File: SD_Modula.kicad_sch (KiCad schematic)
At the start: 6 parts, among them J2 Micro_SD_Card_Det1, U4 74LVC125

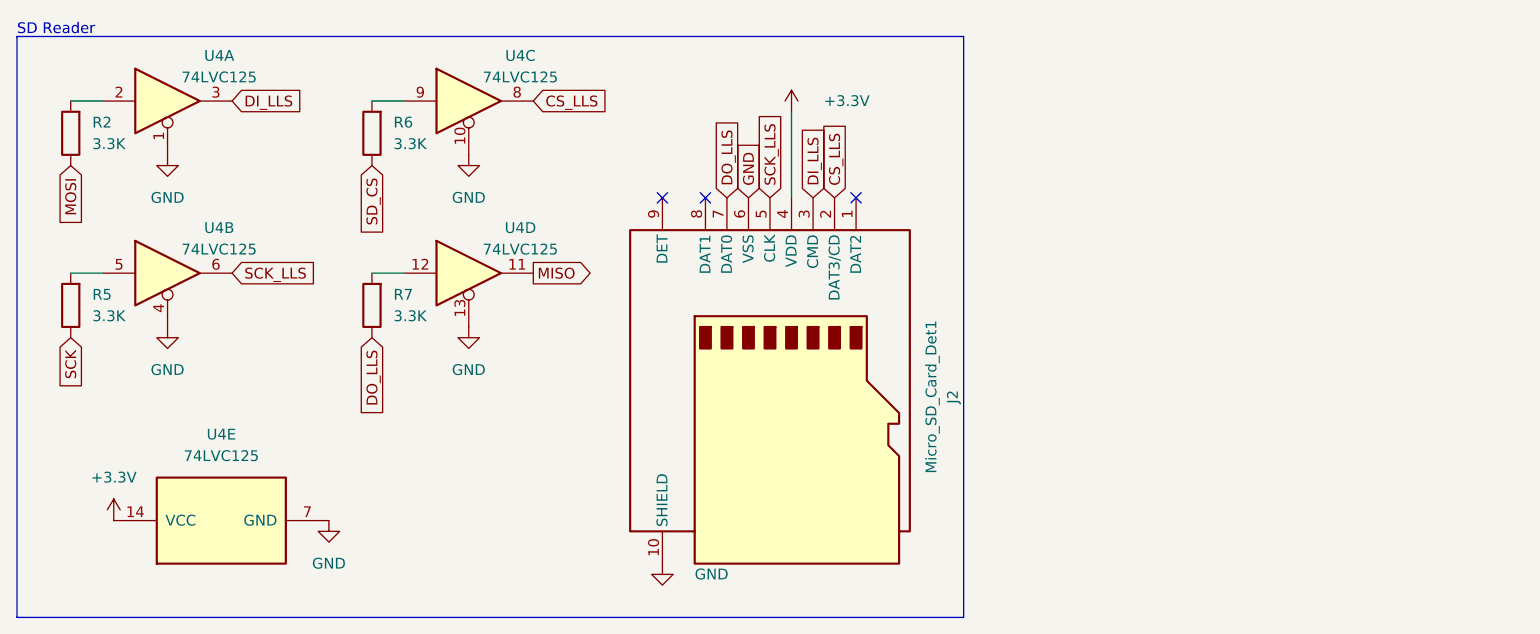
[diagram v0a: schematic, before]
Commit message: added psu and formated board outline
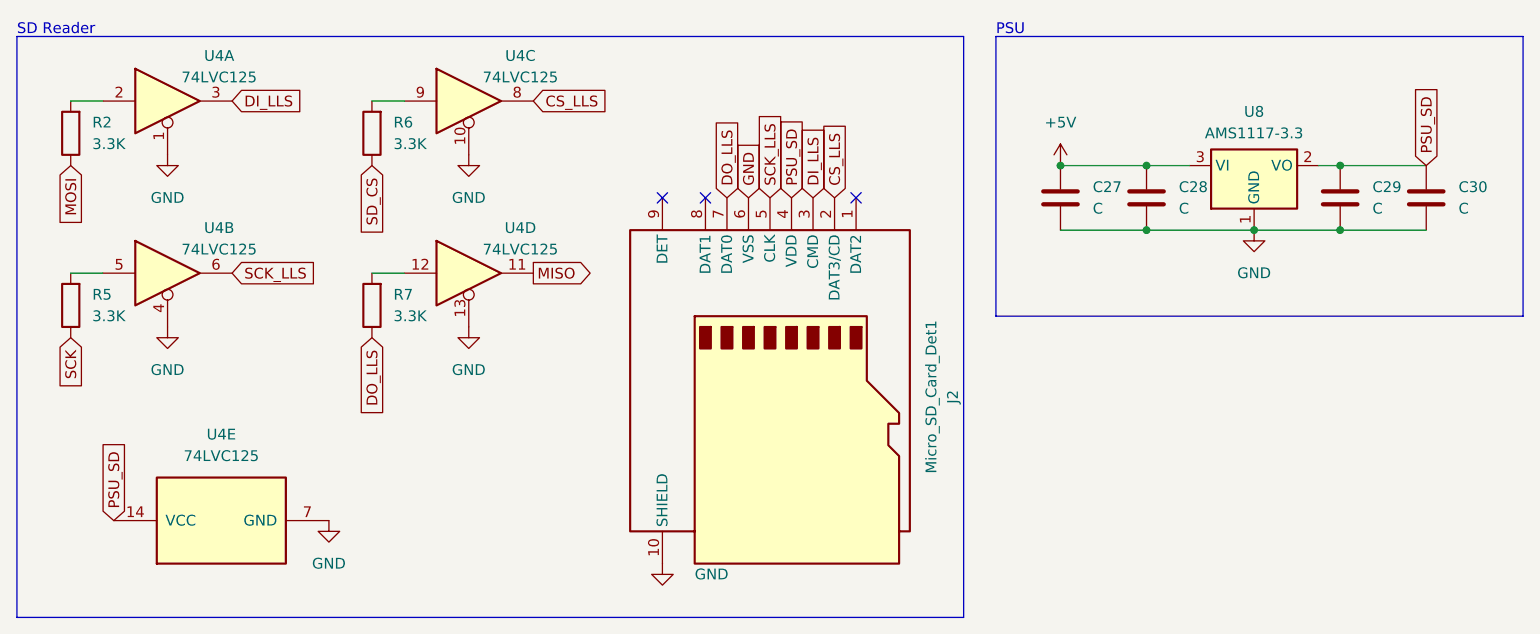
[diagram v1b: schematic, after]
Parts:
- added C27, C28, C29, C30: C, symbol Device:C
- added U8: AMS1117-3.3, Package_TO_SOT_SMD:SOT-223-3_TabPin2, symbol Regulator_Linear:AMS1117-3.3
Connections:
- net GND: now also C27.2, C28.2, C29.2, C30.2, U8.1 (GND)
- net +3.3V renamed PSU_SD
- net PSU_SD: now also C29.1, C30.1, U8.2 (VO)
- new net +5V: C27.1, C28.1, U8.3 (VI)
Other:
- note added: "PSU"

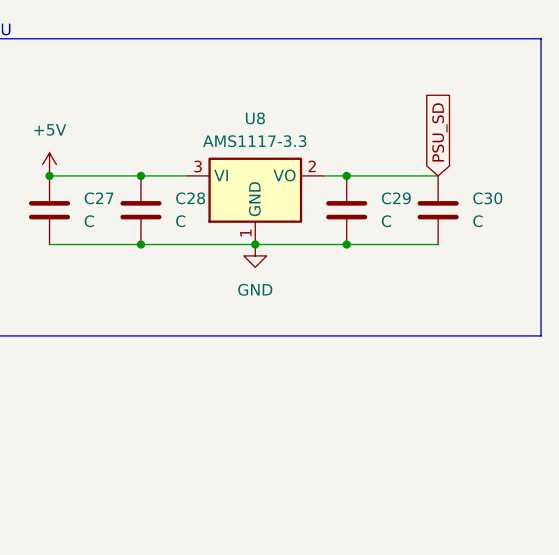
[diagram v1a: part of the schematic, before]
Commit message: added footprint for a7670e
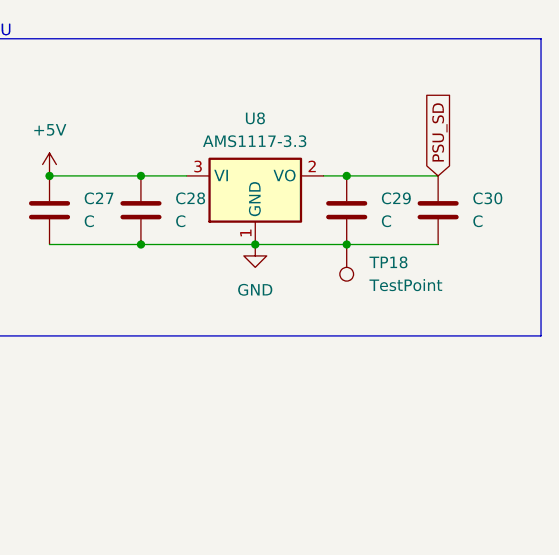
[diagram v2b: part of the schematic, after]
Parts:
- added TP18: TestPoint, symbol Connector:TestPoint
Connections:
- net GND: now also TP18.1
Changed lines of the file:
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@@
+	)
+	(symbol
+		(lib_id "Connector:TestPoint")
+		(at 173.99 40.64 180)
+		(unit 1)
+		(exclude_from_sim no)
+		(in_bom yes)
+		(on_board yes)
+		(dnp no)
+		(fields_autoplaced yes)
+		(property "Reference" "TP18"
+			(at 176.53 42.6719 0)
+			(effects
+				(font
+					(size 1.27 1.27)
+				)
+				(justify right)
+			)
+		)
+		(property "Value" "TestPoint"
+			(at 176.53 45.2119 0)
+			(effects
+				(font
+					(size 1.27 1.27)
+				)
+				(justify right)
+			)
+		)
+		(property "Footprint" ""
+			(at 168.91 40.64 0)
+			(effects
+				(font
+					(size 1.27 1.27)
+				)
+				(hide yes)
+			)
+		)
+		(property "Datasheet" "~"
+			(at 168.91 40.64 0)
+			(effects
+				(font
+					(size 1.27 1.27)
+				)
+				(hide yes)
+			)
+		)
+		(property "Description" "test point"
+			(at 173.99 40.64 0)
+			(effects
+				(font
+					(size 1.27 1.27)
+				)
+				(hide yes)
+			)
+		)
+		(pin "1"
+		)
+		(instances
+			(project "Hardware"
+				(path "/f04ee758-a926-48b7-b458-286a696c3ef4/9702ddf2-9814-4139-b4ef-da102dfdd360"
+					(reference "TP18")
+					(unit 1)
+				)
+			)
+		)
 	)
 	(symbol

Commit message: done most of the schematics
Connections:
- net PSU_SD renamed PSU
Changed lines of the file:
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@@
+		)
+	)
+	(wire
+		(pts
+			(xy 109.22 25.4) (xy 109.22 36.83)
+		)
+		(stroke
+			(width 0)
+			(type default)
 		)
 	)
@@
 		)
 	)
+	(label "PSU"
+		(at 184.15 33.02 180)
+		(fields_autoplaced yes)
+		(effects
+			(font
+				(size 1.27 1.27)
+			)
+			(justify right bottom)
+		)
+	)
+	(label "PSU"
+		(at 29.21 74.93 180)
+		(fields_autoplaced yes)
+		(effects
+			(font
+				(size 1.27 1.27)
+			)
+			(justify right bottom)
+		)
+	)
+	(label "PSU"
+		(at 109.22 25.4 90)
+		(fields_autoplaced yes)
+		(effects
+			(font
+				(size 1.27 1.27)
+			)
+			(justify left bottom)
+		)
+	)
 	(global_label "SCK_LLS"
 		(shape input)
@@
 		(property "Intersheetrefs" "${INTERSHEET_REFS}"
 			(at 106.68 25.862 90)
-			(effects
-				(font
-					(size 1.27 1.27)
-				)
-				(justify left)
-				(hide yes)
-			)
-		)
-	)
-	(global_label "PSU_SD"
-		(shape input)
-		(at 29.21 74.93 90)
-		(fields_autoplaced yes)
-		(effects
-			(font
-				(size 1.27 1.27)
-			)
-			(justify left)
-		)
-		(property "Intersheetrefs" "${INTERSHEET_REFS}"
-			(at 29.21 64.6877 90)
 			(effects
 				(font
@@
 		)
 	)
-	(global_label "PSU_SD"
-		(shape input)
-		(at 184.15 33.02 90)
-		(fields_autoplaced yes)
-		(effects
-			(font
-				(size 1.27 1.27)
-			)
-			(justify left)
-		)
-		(property "Intersheetrefs" "${INTERSHEET_REFS}"
-			(at 184.15 22.7777 90)
-			(effects
-				(font
-					(size 1.27 1.27)
-				)
-				(justify left)
-				(hide yes)
-			)
-		)
-	)
 	(global_label "SD_CS"
 		(shape input)
@@
 			(effects
 				(font
-					(size 1.27 1.27)
-				)
-				(justify left)
-				(hide yes)
-			)
-		)
-	)
-	(global_label "PSU_SD"
-		(shape input)
-		(at 109.22 36.83 90)
-		(fields_autoplaced yes)
-		(effects
-			(font
-				(size 1.27 1.27)
-			)
-			(justify left)
-		)
-		(property "Intersheetrefs" "${INTERSHEET_REFS}"
-			(at 109.22 26.5877 90)
-			(effects
-				(font

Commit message: done refacoring
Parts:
- C27, C29: value C -> 10uF
- C28, C30: value C -> 100pF
- TP18: footprint (none) -> TestPoint:TestPoint_Pad_D2.5mm

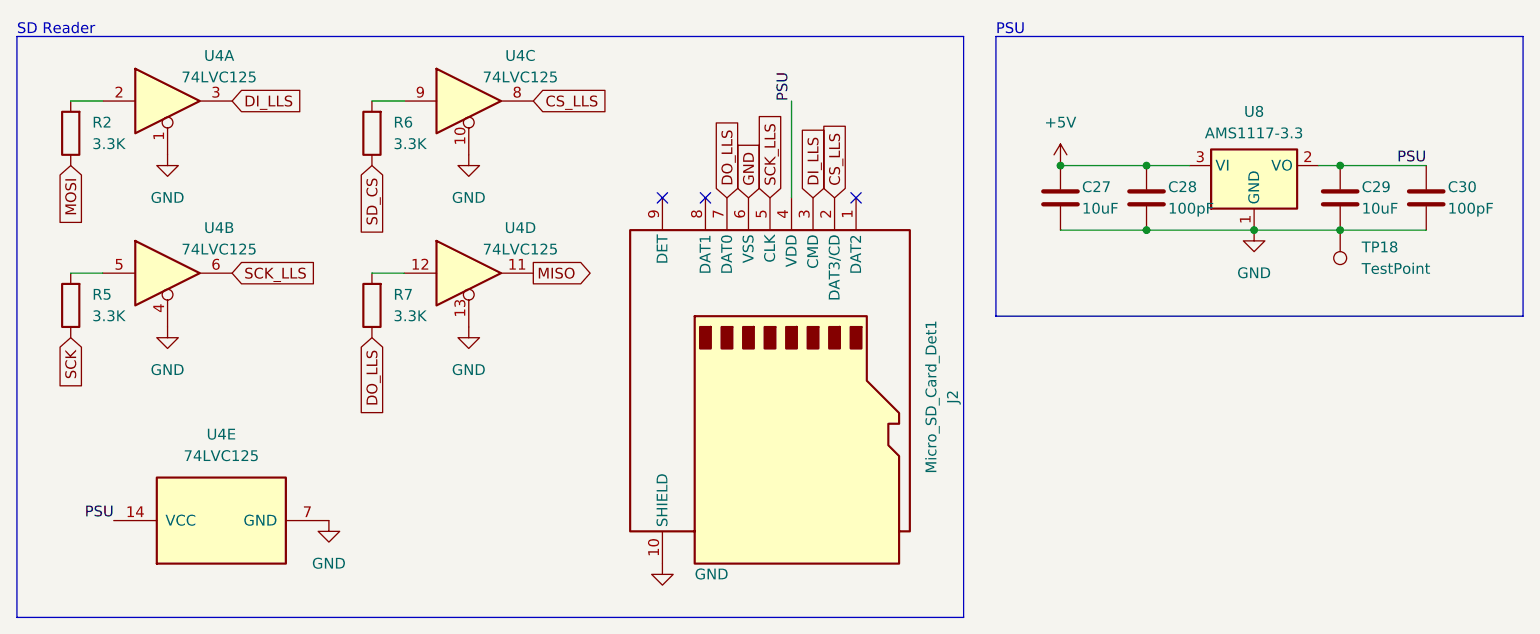
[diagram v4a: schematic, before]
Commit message: assigned most footprints
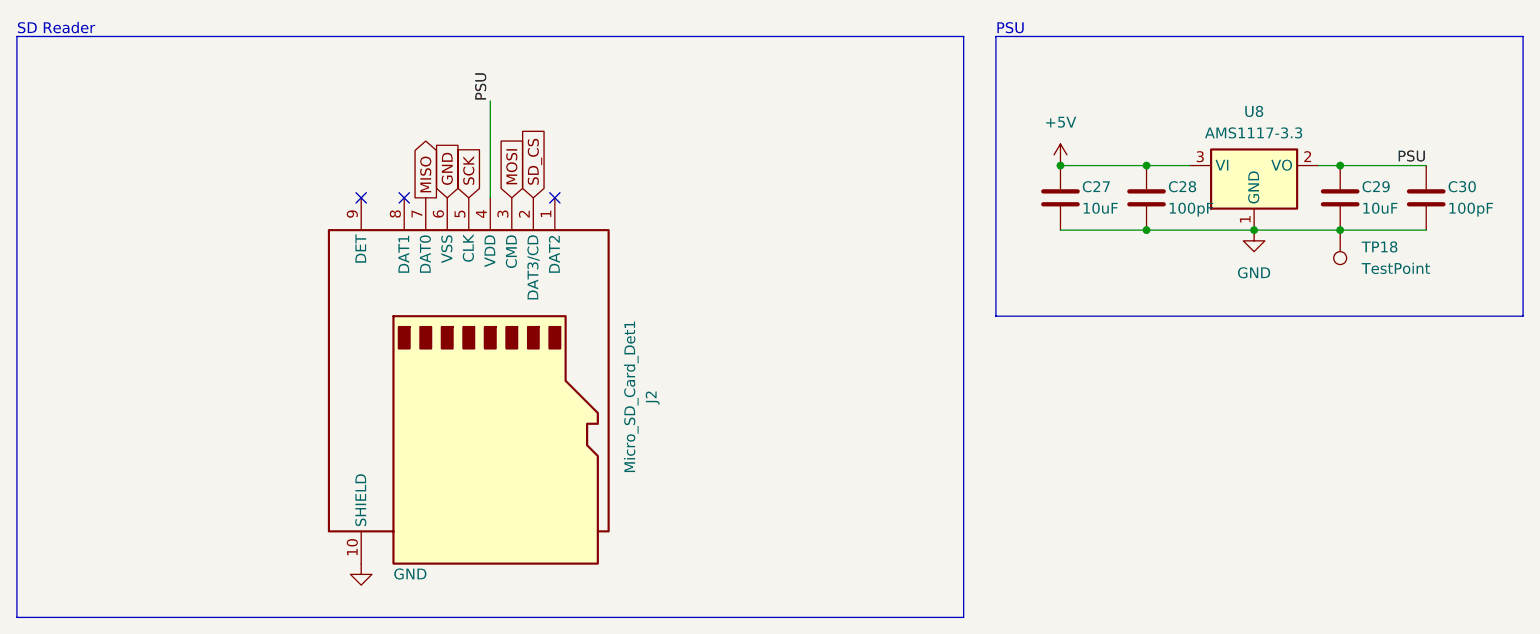
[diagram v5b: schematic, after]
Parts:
- removed R2, R5, R6, R7: 3.3K, symbol Device:R
- removed U4: 74LVC125, symbol 74xx:74LVC125
- J2: footprint (none) -> 3M_SD-RSMT-2-MQ-WF:3M_SD-RSMT-2-MQ-WF
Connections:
- net CS_LLS is gone; now on net SD_CS: J2.2 (DAT3/CD)
- net DI_LLS is gone; now on net MOSI: J2.3 (CMD)
- net DO_LLS is gone; now on net MISO: J2.7 (DAT0)
- net SCK_LLS is gone; now on net SCK: J2.5 (CLK)
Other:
- moved on the sheet: J2

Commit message: cleaned up scematics and updated power management
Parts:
- C27, C29: footprint (none) -> Capacitor_SMD:C_1206_3216Metric
- C28, C30: footprint (none) -> Capacitor_SMD:C_0805_2012Metric

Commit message: finelized scematics
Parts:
- removed J2: Micro_SD_Card_Det1, 3M_SD-RSMT-2-MQ-WF:3M_SD-RSMT-2-MQ-WF, symbol Connector:Micro_SD_Card_Det1
- added J6: Micro_SD_Card, Connector_Card:microSD_HC_Hirose_DM3BT-DSF-PEJS, symbol Connector:Micro_SD_Card
- TP18: footprint TestPoint:TestPoint_Pad_D2.5mm -> TestPoint:TestPoint_Pad_D2.0mm
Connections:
- net GND: now also J6.6 (VSS), J6.9 (SHIELD)
- net MISO: now also J6.7 (DAT0)
- net MOSI: now also J6.3 (CMD)
- net PSU: now also J6.4 (VDD)
- net SCK: now also J6.5 (CLK)
- net SD_CS: now also J6.2 (DAT3/CD)
- no-connect marks 3 -> 2
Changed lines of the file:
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@@
 		(at 63.5 36.83)
-	)
-	(no_connect
-		(at 58.42 36.83)
 	)
 	(wire
@@
 	)
 	(symbol
+		(lib_id "Connector:Micro_SD_Card")
+		(at 73.66 59.69 270)
+		(unit 1)
+		(exclude_from_sim no)
+		(in_bom yes)
+		(on_board yes)
+		(dnp no)
+		(fields_autoplaced yes)
+		(property "Reference" "J6"
+			(at 88.9 59.0549 90)
+			(effects
+				(font
+					(size 1.27 1.27)
+				)
+				(justify left)
+			)
+		)
+		(property "Value" "Micro_SD_Card"
+			(at 88.9 61.5949 90)
+			(effects
+				(font
+					(size 1.27 1.27)
+				)
+				(justify left)
+			)
+		)
+		(property "Footprint" "Connector_Card:microSD_HC_Hirose_DM3BT-DSF-PEJS"
+			(at 81.28 88.9 0)
+			(effects
+				(font
+					(size 1.27 1.27)
+				)
+				(hide yes)
+			)
+		)
+		(property "Datasheet" "http://katalog.we-online.de/em/datasheet/693072010801.pdf"
+			(at 73.66 59.69 0)
+			(effects
+				(font
+					(size 1.27 1.27)
+				)
+				(hide yes)
+			)
+		)
+		(property "Description" "Micro SD Card Socket"
+			(at 73.66 59.69 0)
+			(effects
+				(font
+					(size 1.27 1.27)
+				)
+				(hide yes)
+			)
+		)
+		(pin "2"
+		)
+		(pin "8"
+		)
+		(pin "7"
+		)
+		(pin "5"
+		)
+		(pin "3"
+		)
+		(pin "1"
+		)
+		(pin "4"
+		)
+		(pin "6"
+		)
+		(pin "9"
+		)
+		(instances
+			(project "Hardware"
+				(path "/f04ee758-a926-48b7-b458-286a696c3ef4/9702ddf2-9814-4139-b4ef-da102dfdd360"
+					(reference "J6")
+					(unit 1)
+				)
+			)
+		)
+	)
+	(symbol
 		(lib_id "Device:C")
 		(at 151.13 36.83 0)
@@
 	)
 	(symbol
-		(lib_id "Connector:Micro_SD_Card_Det1")
-		(at 71.12 59.69 270)
-		(unit 1)
-		(exclude_from_sim no)
-		(in_bom yes)
-		(on_board yes)
-		(dnp no)
-		(fields_autoplaced yes)
-		(property "Reference" "J2"
-			(at 92.71 60.325 0)
-			(effects
-				(font
-					(size 1.27 1.27)
-				)
-			)
-		)
-		(property "Value" "Micro_SD_Card_Det1"
-			(at 90.17 60.325 0)
-			(effects
-				(font
-					(size 1.27 1.27)
-				)
-			)
-		)
-		(property "Footprint" "3M_SD-RSMT-2-MQ-WF:3M_SD-RSMT-2-MQ-WF"
-			(at 88.9 111.76 0)
-			(effects
-				(font
-					(size 1.27 1.27)
-				)
-				(hide yes)
-			)
-		)
-		(property "Datasheet" "https://datasheet.lcsc.com/lcsc/2110151630_XKB-Connectivity-XKTF-015-N_C381082.pdf"
-			(at 73.66 59.69 0)
-			(effects
-				(font
-					(size 1.27 1.27)
-				)
-				(hide yes)
-			)
-		)
-		(property "Description" "Micro SD Card Socket with one card detection pin"
-			(at 71.12 59.69 0)
-			(effects
-				(font
-					(size 1.27 1.27)
-				)
-				(hide yes)
-			)
-		)
-		(property "Availability" ""
-			(at 71.12 59.69 0)
-			(effects
-				(font
-					(size 1.27 1.27)
-				)
-				(hide yes)
-			)
-		)
-		(property "Check_prices" ""
-			(at 71.12 59.69 0)
-			(effects
-				(font
-					(size 1.27 1.27)
-				)
-				(hide yes)
-			)
-		)
-		(property "Description_1" ""
-			(at 71.12 59.69 0)
-			(effects
-				(font
-					(size 1.27 1.27)
-				)
-				(hide yes)
-			)
-		)
-		(property "MANUFACTURER" ""
-			(at 71.12 59.69 0)
-			(effects
-				(font
-					(size 1.27 1.27)
-				)
-				(hide yes)
-			)
-		)
-		(property "MAXIMUM_PACKAGE_HEIGHT" ""
-			(at 71.12 59.69 0)
-			(effects
-				(font
-					(size 1.27 1.27)
-				)
-				(hide yes)
-			)
-		)
-		(property "MF" ""
-			(at 71.12 59.69 0)
-			(effects
-				(font
-					(size 1.27 1.27)
-				)
-				(hide yes)
-			)
-		)
-		(property "MP" ""
-			(at 71.12 59.69 0)
-			(effects
-				(font
-					(size 1.27 1.27)
-				)
-				(hide yes)
-			)
-		)
-		(property "PARTREV" ""
-			(at 71.12 59.69 0)
-			(effects
-				(font
-					(size 1.27 1.27)
-				)
-				(hide yes)
-			)
-		)
-		(property "Package" ""
-			(at 71.12 59.69 0)
-			(effects
-				(font
-					(size 1.27 1.27)
-				)
-				(hide yes)
-			)
-		)
-		(property "Price" ""
-			(at 71.12 59.69 0)
-			(effects
-				(font
-					(size 1.27 1.27)
-				)
-				(hide yes)
-			)
-		)
-		(property "SNAPEDA_PN" ""
-			(at 71.12 59.69 0)
-			(effects
-				(font
-					(size 1.27 1.27)
-				)
-				(hide yes)
-			)
-		)
-		(property "STANDARD" ""
-			(at 71.12 59.69 0)
-			(effects
-				(font
-					(size 1.27 1.27)
-				)
-				(hide yes)
-			)
-		)
-		(property "SnapEDA_Link" ""
-			(at 71.12 59.69 0)
-			(effects
-				(font
-					(size 1.27 1.27)
-				)
-				(hide yes)
-			)
-		)
-		(pin "1"
-		)
-		(pin "9"
-		)
-		(pin "6"
-		)
-		(pin "7"
-		)
-		(pin "3"
-		)
-		(pin "8"
-		)
-		(pin "5"
-		)
-		(pin "2"
-		)
-		(pin "4"
-		)
-		(pin "10"
-		)
-		(instances
-			(project "Hardware"
-				(path "/f04ee758-a926-48b7-b458-286a696c3ef4/9702ddf2-9814-4139-b4ef-da102dfdd360"
-					(reference "J2")
-					(unit 1)
-				)
-			)
-		)
-	)
-	(symbol
 		(lib_id "Connector:TestPoint")
 		(at 173.99 40.64 180)
@@
 			)
 		)
-		(property "Footprint" "TestPoint:TestPoint_Pad_D2.5mm"
+		(property "Footprint" "TestPoint:TestPoint_Pad_D2.0mm"
 			(at 168.91 40.64 0)
 			(effects

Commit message: mostly layouted
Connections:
- net GND: no longer TP18.1
- net PSU: now also TP18.1
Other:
- moved on the sheet: TP18
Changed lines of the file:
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@@
+		)
+	)
+	(wire
+		(pts
+			(xy 173.99 30.48) (xy 173.99 33.02)
+		)
+		(stroke
+			(width 0)
+			(type default)
 		)
 	)
@@
 	(symbol
 		(lib_id "Connector:TestPoint")
-		(at 173.99 40.64 180)
+		(at 173.99 30.48 0)
 		(unit 1)
 		(exclude_from_sim no)
@@
 		(fields_autoplaced yes)
 		(property "Reference" "TP18"
-			(at 176.53 42.6719 0)
-			(effects
-				(font
-					(size 1.27 1.27)
-				)
-				(justify right)
+			(at 176.53 25.9079 0)
+			(effects
+				(font
+					(size 1.27 1.27)
+				)
+				(justify left)
 			)
 		)
 		(property "Value" "TestPoint"
-			(at 176.53 45.2119 0)
-			(effects
-				(font
-					(size 1.27 1.27)
-				)
-				(justify right)
+			(at 176.53 28.4479 0)
+			(effects
+				(font
+					(size 1.27 1.27)
+				)
+				(justify left)
 			)
 		)
 		(property "Footprint" "TestPoint:TestPoint_Pad_D2.0mm"
-			(at 168.91 40.64 0)
+			(at 179.07 30.48 0)
 			(effects
 				(font
@@
 		)
 		(property "Datasheet" "~"
-			(at 168.91 40.64 0)
+			(at 179.07 30.48 0)
 			(effects
 				(font
@@
 		)
 		(property "Description" "test point"
-			(at 173.99 40.64 0)
+			(at 173.99 30.48 0)
 			(effects
 				(font
@@
 		)
 		(property "Availability" ""
-			(at 173.99 40.64 0)
+			(at 173.99 30.48 0)
 			(effects
 				(font
@@
 		)
 		(property "Check_prices" ""
-			(at 173.99 40.64 0)
+			(at 173.99 30.48 0)
 			(effects
 				(font
@@
 		)
 		(property "Description_1" ""
-			(at 173.99 40.64 0)
+			(at 173.99 30.48 0)
 			(effects
 				(font
@@
 		)
 		(property "MANUFACTURER" ""
-			(at 173.99 40.64 0)
+			(at 173.99 30.48 0)
 			(effects
 				(font
@@
 		)
 		(property "MAXIMUM_PACKAGE_HEIGHT" ""
-			(at 173.99 40.64 0)
+			(at 173.99 30.48 0)
 			(effects
 				(font
@@
 		)
 		(property "MF" ""
-			(at 173.99 40.64 0)
+			(at 173.99 30.48 0)
 			(effects
 				(font
@@
 		)
 		(property "MP" ""
-			(at 173.99 40.64 0)
+			(at 173.99 30.48 0)
 			(effects
 				(font
@@
 		)
 		(property "PARTREV" ""
-			(at 173.99 40.64 0)
+			(at 173.99 30.48 0)
 			(effects
 				(font
@@
 		)
 		(property "Package" ""
-			(at 173.99 40.64 0)
+			(at 173.99 30.48 0)
 			(effects
 				(font
@@
 		)
 		(property "Price" ""
-			(at 173.99 40.64 0)
+			(at 173.99 30.48 0)
 			(effects
 				(font
@@
 		)
 		(property "SNAPEDA_PN" ""
-			(at 173.99 40.64 0)
+			(at 173.99 30.48 0)
 			(effects
 				(font
@@
 		)
 		(property "STANDARD" ""
-			(at 173.99 40.64 0)
+			(at 173.99 30.48 0)
 			(effects
 				(font
@@
 		)
 		(property "SnapEDA_Link" ""
-			(at 173.99 40.64 0)
-			(effects
-				(font
+			(at 173.99 30.48 0)
+			(effects
+				(font
